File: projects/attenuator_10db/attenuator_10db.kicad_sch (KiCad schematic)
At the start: 5 parts, among them J1 SMA_IN, J2 SMA_OUT

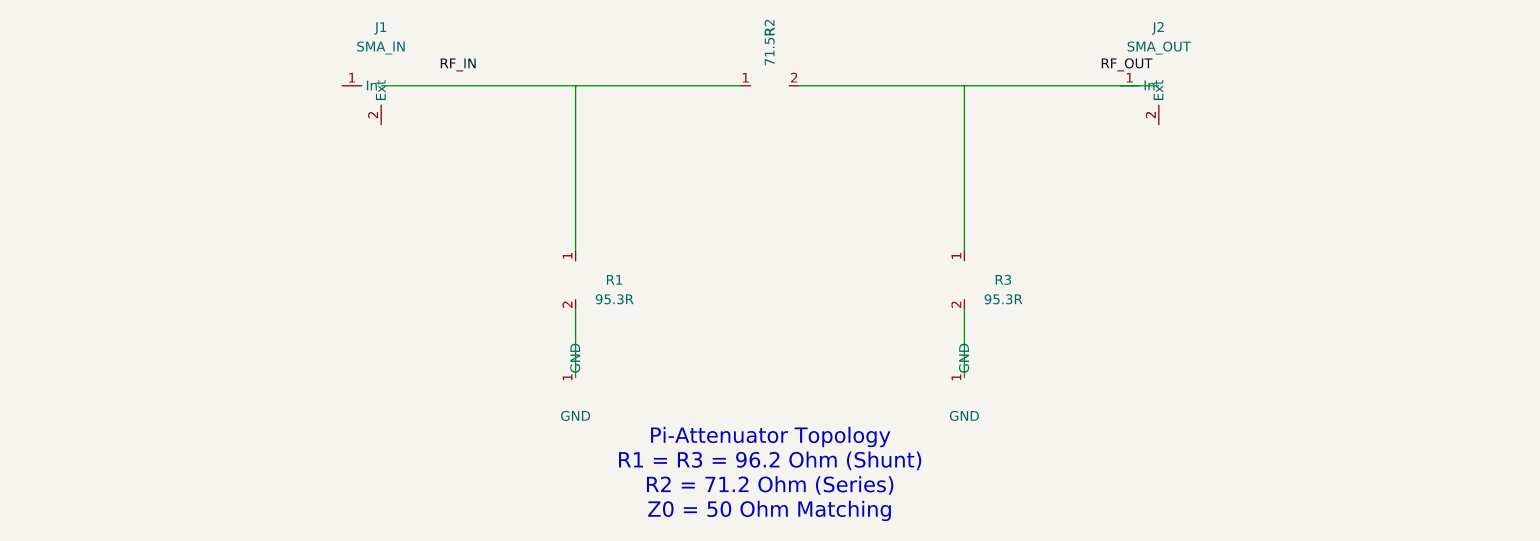
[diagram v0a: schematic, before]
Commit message: feat: implement zoomed schematic render, CPWG controlled impedance synthesis, and custom circuit description parsing
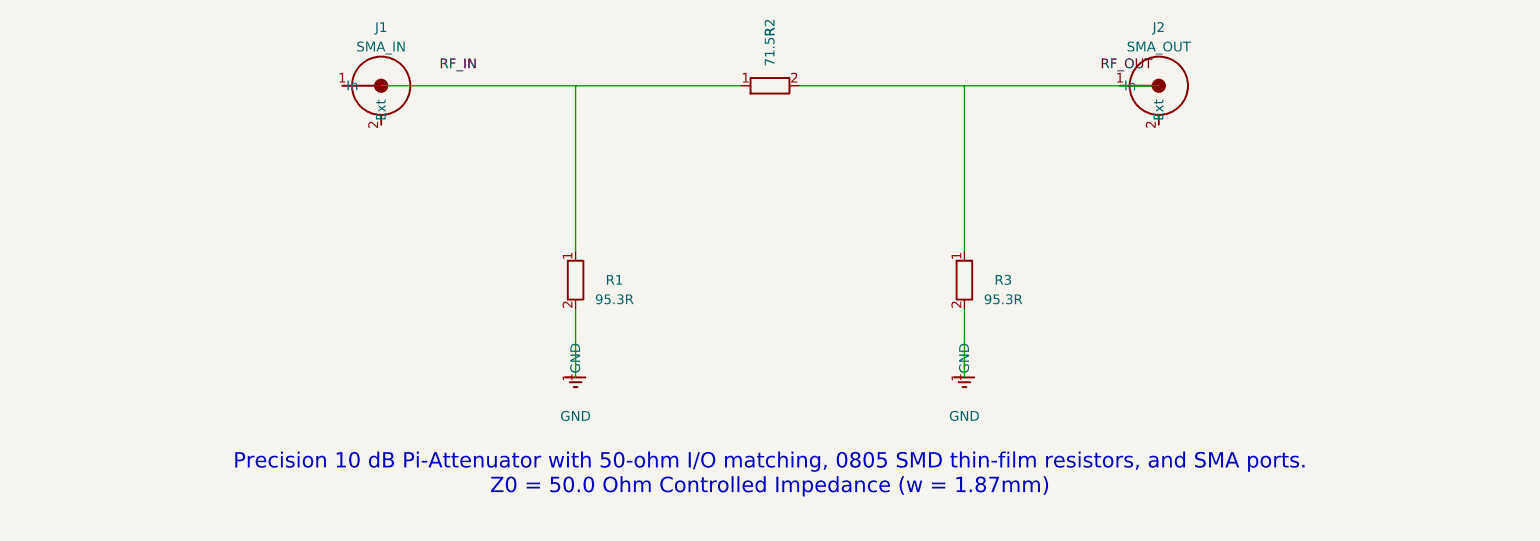
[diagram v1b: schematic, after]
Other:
- note added: "Precision 10 dB Pi-Attenuator with 50-ohm I/O matching, 0805 SMD thin-film resistors, and SMA ports. Z0 = 50.0 Ohm Controlled Impedance (w = 1.87mm)"
- note removed: "Pi-Attenuator Topology R1 = R3 = 96.2 Ohm (Shunt) R2 = 71.2 Ohm (Series) Z0 = 50 Ohm Matching"
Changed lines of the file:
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@@
 		(company "RF AI Suite")
 		(comment 1 "Z0 = 50.0 Ohm | Target S21 = -10.0 dB")
-		(comment 2 "Substrate: FR4 (er=4.4, h=1.6mm)")
+		(comment 2 "Substrate: FR4 (er=4.4, h=1.6mm, w_50=1.87mm)")
 	)
 	(symbol
 		(lib_id "Connector:Conn_Coaxial")
 		(at 38.1 76.2 0)
-		(unit 1)
-		(exclude_from_sim no)
-		(in_bom yes)
-		(on_board yes)
 		(property "Reference" "J1" (at 38.1 68.58 0))
 		(property "Value" "SMA_IN" (at 38.1 71.12 0))
@@
 		(lib_id "Device:R")
 		(at 63.5 101.6 0)
-		(unit 1)
-		(exclude_from_sim no)
-		(in_bom yes)
-		(on_board yes)
 		(property "Reference" "R1" (at 68.58 101.6 0))
 		(property "Value" "95.3R" (at 68.58 104.14 0))
@@
 		(lib_id "Device:R")
 		(at 88.9 76.2 90)
-		(unit 1)
-		(exclude_from_sim no)
-		(in_bom yes)
-		(on_board yes)
 		(property "Reference" "R2" (at 88.9 68.58 0))
 		(property "Value" "71.5R" (at 88.9 71.12 0))
@@
 		(lib_id "Device:R")
 		(at 114.3 101.6 0)
-		(unit 1)
-		(exclude_from_sim no)
-		(in_bom yes)
-		(on_board yes)
 		(property "Reference" "R3" (at 119.38 101.6 0))
 		(property "Value" "95.3R" (at 119.38 104.14 0))
@@
 		(lib_id "Connector:Conn_Coaxial")
 		(at 139.7 76.2 0)
-		(unit 1)
-		(exclude_from_sim no)
-		(in_bom yes)
-		(on_board yes)
 		(property "Reference" "J2" (at 139.7 68.58 0))
 		(property "Value" "SMA_OUT" (at 139.7 71.12 0))
@@
 	(label "RF_IN" (at 45.72 73.66 0))
 	(label "RF_OUT" (at 132.08 73.66 0))
-	(text "Pi-Attenuator Topology\nR1 = R3 = 96.2 Ohm (Shunt)\nR2 = 71.2 Ohm (Series)\nZ0 = 50 Ohm Matching" (at 88.9 127.0 0) (effects (font (size 2.0 2.0))))
+	(text "Precision 10 dB Pi-Attenuator with 50-ohm I/O matching, 0805 SMD thin-film resistors, and SMA ports.\nZ0 = 50.0 Ohm Controlled Impedance (w = 1.87mm)" (at 88.9 127.0 0) (effects (font (size 2.0 2.0))))
 )
